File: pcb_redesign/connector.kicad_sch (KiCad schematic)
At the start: 8 parts, among them J1 USB_B_Mini, U2 ?

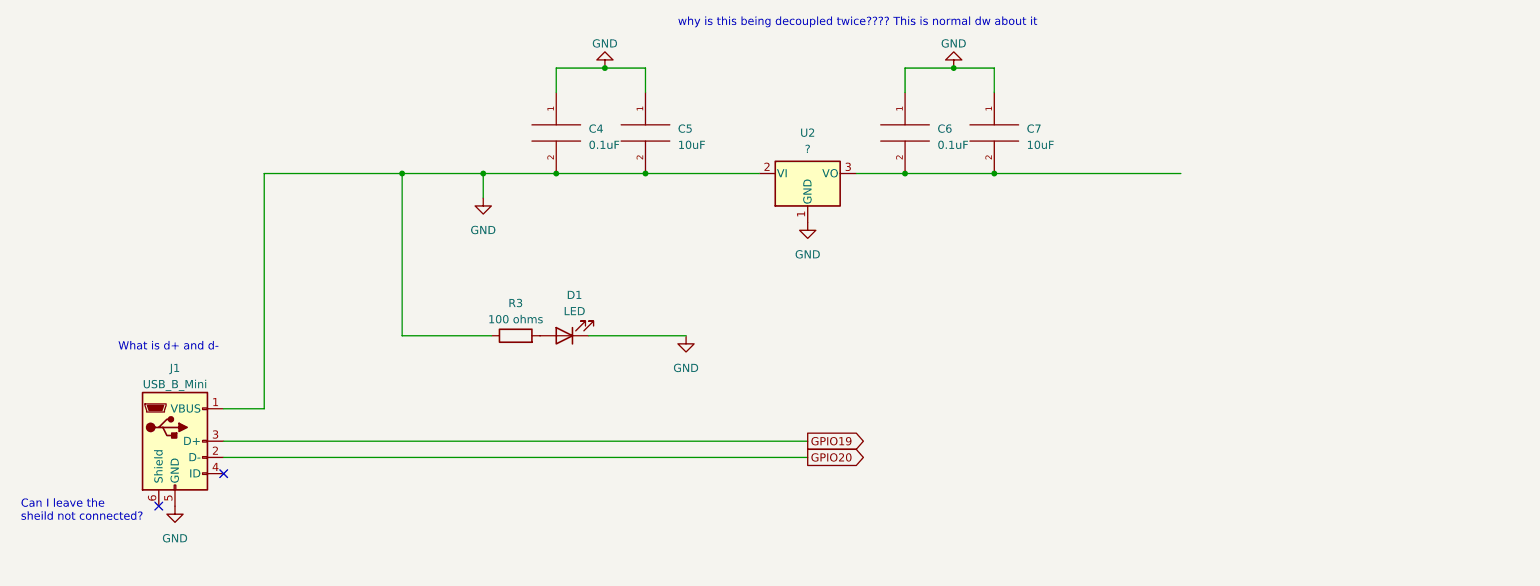
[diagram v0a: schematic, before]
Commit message: schematic imported
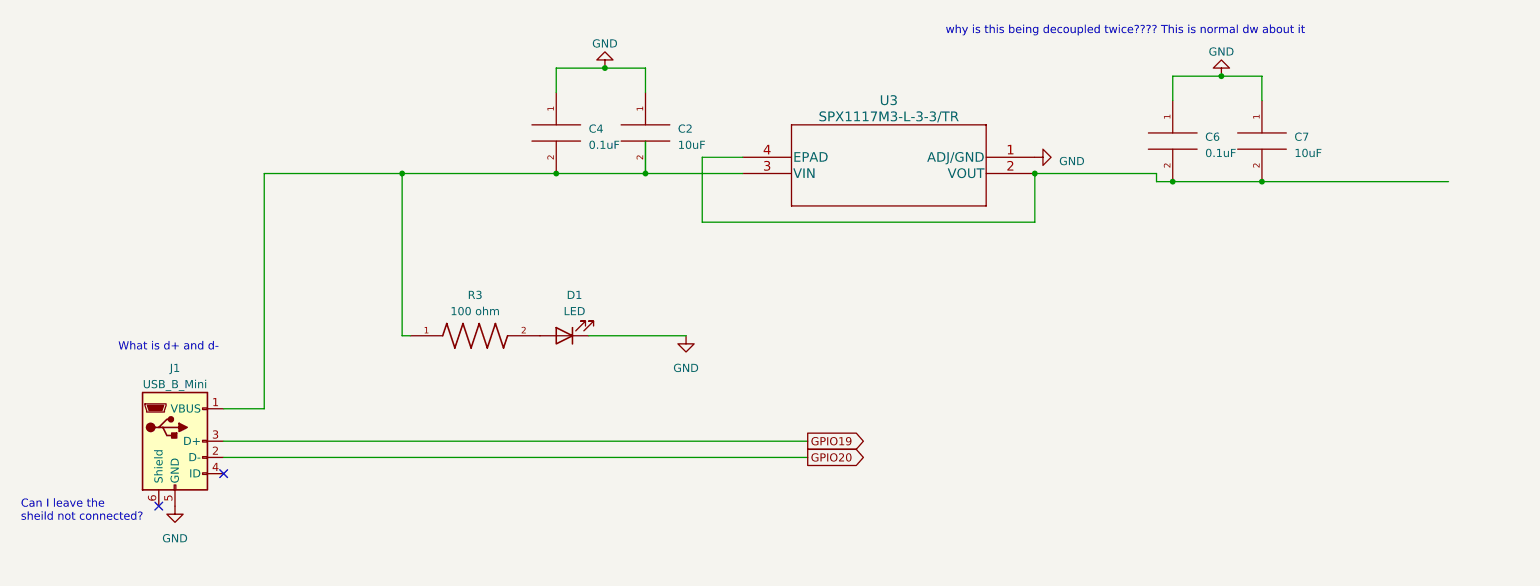
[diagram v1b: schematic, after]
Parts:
- removed C5: 10uF, symbol pspice:C
- removed R3: 100 ohms, symbol Device:R
- removed U2: ?, symbol Regulator_Linear:L7912
- added C2: 10uF, 10uF_cap_0603:CAPC1608X90N, symbol pspice:C
- added R3: 100 ohm, RESC1608X50N, symbol 100_ohm_0603:RR0816P-101-D
- added U3: SPX1117M3-L-3-3/TR, 3.3v_reg:SPX1117M3-L-3-3&slash_TR, symbol 3.3v_reg:SPX1117M3-L-3-3/TR
- C4: footprint (none) -> 1uF_cap_0603:CL10A105KB8NNNC
- C6: footprint (none) -> 0.1uF_cap_0603:CAPC1608X90N
- C7: footprint (none) -> 10uF_cap_0603:CAPC1608X90N
- D1: footprint (none) -> green_LED:LEDC2012X70N
- J1: footprint (none) -> micro_usb_type_b:AMPHENOL_10118192-0002LF
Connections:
- net GND: now also C2.1, U3.1 (ADJ/GND); no longer C4.2, J1.1 (VBUS)
- net at D1.2 (A): now also R3.2
- net at C6.2, C7.2: now also U3.2 (VOUT), U3.4 (EPAD)
- new net: C2.2, C4.2, J1.1 (VBUS), R3.1, U3.3 (VIN)
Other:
- moved on the sheet: C6, C7

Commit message: components added to board
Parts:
- removed J1: USB_B_Mini, micro_usb_type_b:AMPHENOL_10118192-0002LF, symbol Connector:USB_B_Mini
- added J2: USB_B, micro_usb_type_b:AMPHENOL_10118192-0002LF, symbol Connector:USB_B
- D1: footprint green_LED:LEDC2012X70N -> LED_SMD:LED_0805_2012Metric
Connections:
- net GND: now also J2.4 (GND)
- net 3.7_UNREG: now reaches C2.2, C4.2, R3.1, U3.3 (VIN)
- net 3.7_UNREG: now also J2.1 (VBUS)
- net VCC_3V3: now reaches C6.2, C7.2, U3.2 (VOUT), U3.4 (EPAD)
- new net D+: J2.3 (D+)
- new net D-: J2.2 (D-)
- no-connect marks 2 -> 1
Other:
- note added: "note: vet the circuit and make sure getting 5v from vbus wont detonate ur components"
- note removed: "why is this being decoupled twice???? This is normal dw about it"

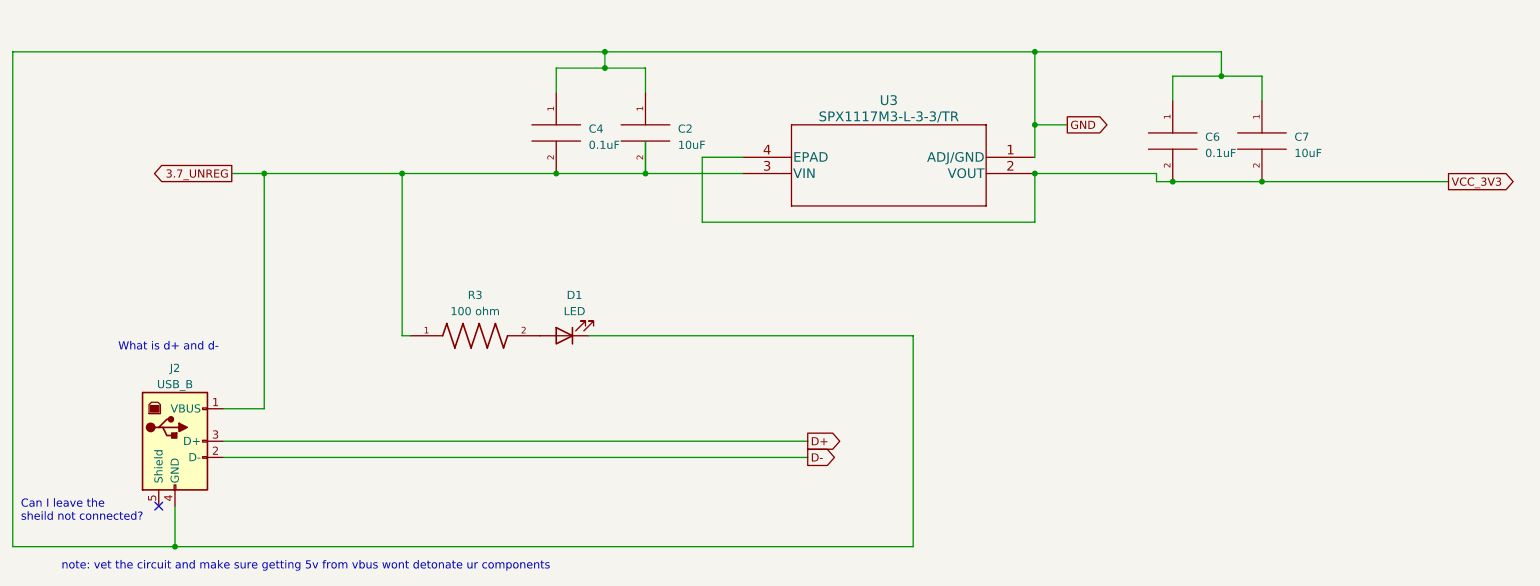
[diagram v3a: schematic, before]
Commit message: wired up 2.13
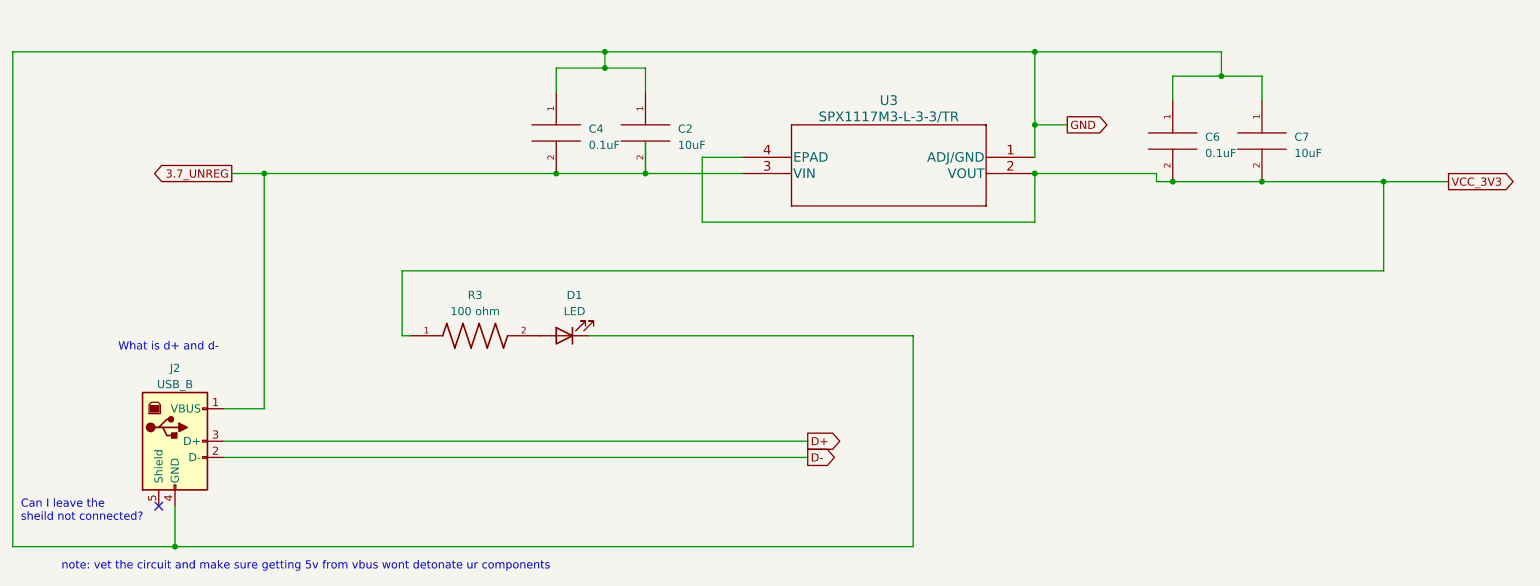
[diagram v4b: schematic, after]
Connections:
- net 3.7_UNREG: no longer R3.1
- net VCC_3V3: now also R3.1
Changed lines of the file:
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@@
   (junction (at 177.8 35.56) (diameter 0) (color 0 0 0 0)
-  )
-  (junction (at 78.74 54.61) (diameter 0) (color 0 0 0 0)
   )
   (junction (at 102.87 54.61) (diameter 0) (color 0 0 0 0)
   )
   (junction (at 57.15 54.61) (diameter 0) (color 0 0 0 0)
+  )
+  (junction (at 232.41 55.88) (diameter 0) (color 0 0 0 0)
   )
   (junction (at 116.84 54.61) (diameter 0) (color 0 0 0 0)
@@
     (stroke (width 0) (type default))
   )
+  (wire (pts (xy 78.74 69.85) (xy 78.74 80.01))
+    (stroke (width 0) (type default))
+  )
   (wire (pts (xy 199.39 39.37) (xy 207.01 39.37))
     (stroke (width 0) (type default))
@@
   )
   (wire (pts (xy 110.49 38.1) (xy 116.84 38.1))
+    (stroke (width 0) (type default))
+  )
+  (wire (pts (xy 232.41 69.85) (xy 78.74 69.85))
     (stroke (width 0) (type default))
   )
@@
     (stroke (width 0) (type default))
   )
-  (wire (pts (xy 57.15 54.61) (xy 78.74 54.61))
+  (wire (pts (xy 57.15 54.61) (xy 102.87 54.61))
     (stroke (width 0) (type default))
   )
@@
     (stroke (width 0) (type default))
   )
-  (wire (pts (xy 78.74 54.61) (xy 102.87 54.61))
+  (wire (pts (xy 207.01 35.56) (xy 207.01 39.37))
     (stroke (width 0) (type default))
   )
-  (wire (pts (xy 207.01 35.56) (xy 207.01 39.37))
+  (wire (pts (xy 232.41 55.88) (xy 232.41 69.85))
     (stroke (width 0) (type default))
   )
@@
     (stroke (width 0) (type default))
   )
-  (wire (pts (xy 78.74 80.01) (xy 78.74 54.61))
+  (wire (pts (xy 232.41 55.88) (xy 242.57 55.88))
     (stroke (width 0) (type default))
   )
@@
     (stroke (width 0) (type default))
   )
-  (wire (pts (xy 213.36 55.88) (xy 242.57 55.88))
+  (wire (pts (xy 213.36 55.88) (xy 232.41 55.88))
     (stroke (width 0) (type default))
   )
